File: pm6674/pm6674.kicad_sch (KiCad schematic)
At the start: 35 parts, among them IC101 ADR434BRZ, J101 Conn_01x10_Pin, U101 LM317_SOT-223, X101 CTS 970

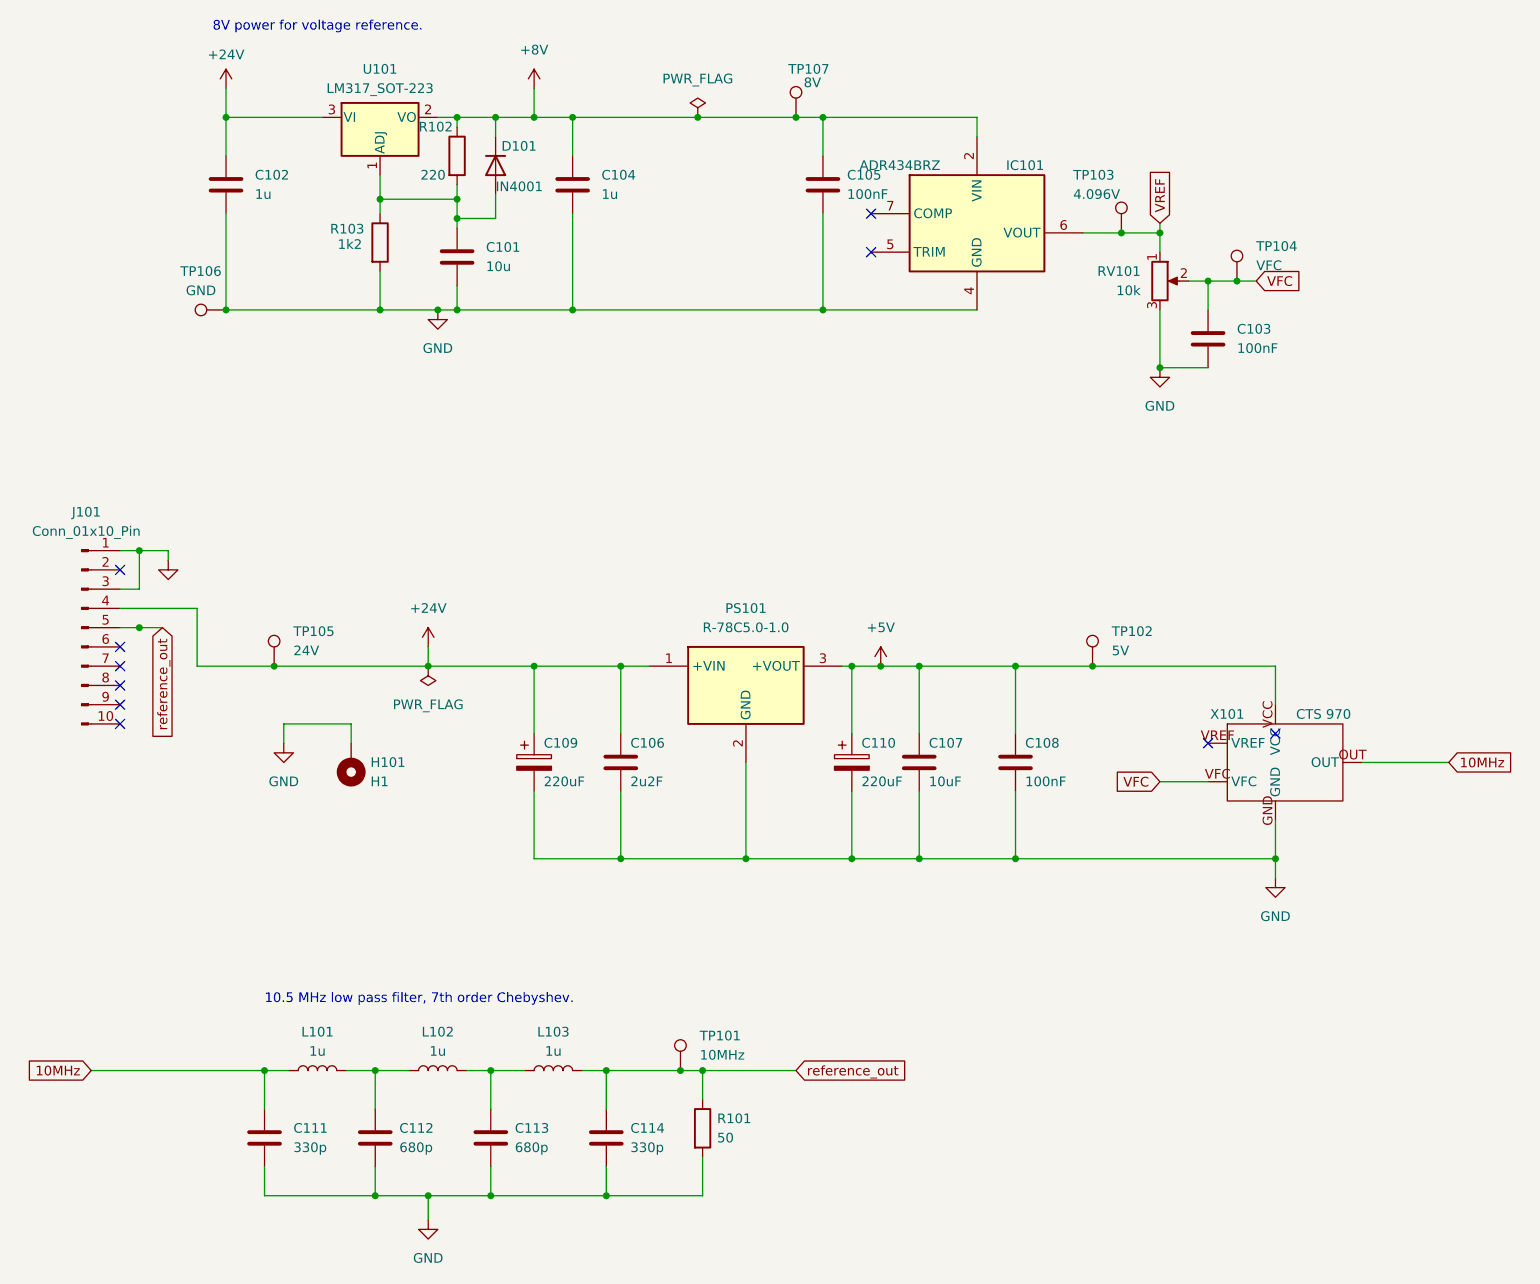
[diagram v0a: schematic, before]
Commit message: Final schematics of built-up and tested board.
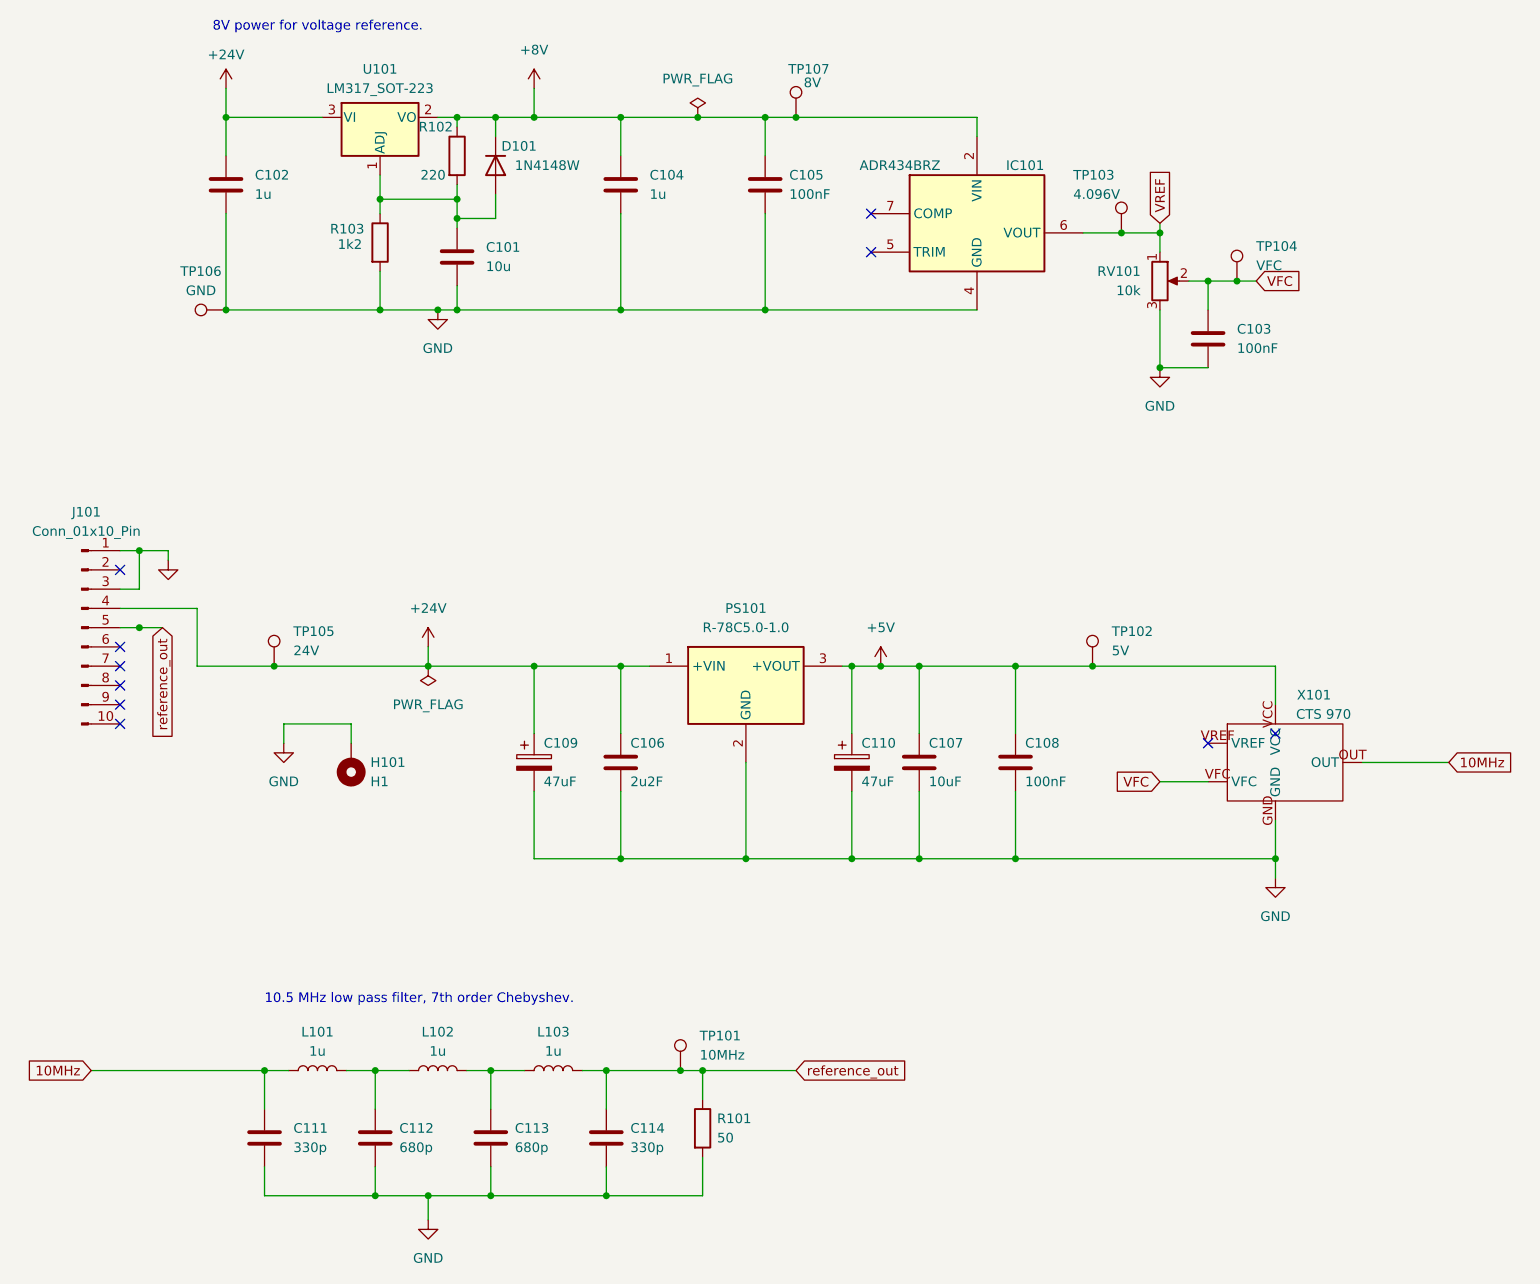
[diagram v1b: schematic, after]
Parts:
- C109, C110: value 220uF -> 47uF
- D101: value IN4001 -> 1N4148W
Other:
- company: Statsøkonomen -> Erik Ø. Sørensen, LB3TH
- moved on the sheet: C104, C105
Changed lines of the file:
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@@
   (title_block
     (title "10MHz reference board for Philips counter PM6674")
-    (company "Statsøkonomen")
+    (date "2023-12-20")
+    (company "Erik Ø. Sørensen, LB3TH")
+    (comment 1 "Inspiration (and physical measurements) from The Sync Channel Blog.")
+    (comment 2 "https://syncchannel.blogspot.com/2016/04/flukephilips-pm66xx-frequency-counter.html")
   )
   (junction (at 162.56 104.14) (diameter 0) (color 0 0 0 0)
@@
   (junction (at 78.105 157.48) (diameter 0) (color 0 0 0 0)
   )
+  (junction (at 129.54 31.75) (diameter 0) (color 0 0 0 0)
+  )
   (junction (at 187.96 53.34) (diameter 0) (color 0 0 0 0)
   )
-  (junction (at 104.14 31.75) (diameter 0) (color 0 0 0 0)
-  )
-  (junction (at 104.14 57.15) (diameter 0) (color 0 0 0 0)
-  )
   (junction (at 181.61 64.77) (diameter 0) (color 0 0 0 0)
   )
@@
   (junction (at 133.604 31.75) (diameter 0) (color 0 0 0 0)
   )
+  (junction (at 110.49 31.75) (diameter 0) (color 0 0 0 0)
+  )
   (junction (at 108.585 157.48) (diameter 0) (color 0 0 0 0)
   )
-  (junction (at 137.16 31.75) (diameter 0) (color 0 0 0 0)
-  )
   (junction (at 88.9 31.75) (diameter 0) (color 0 0 0 0)
   )
   (junction (at 144.78 104.14) (diameter 0) (color 0 0 0 0)
   )
+  (junction (at 110.49 57.15) (diameter 0) (color 0 0 0 0)
+  )
   (junction (at 88.9 42.545) (diameter 0) (color 0 0 0 0)
   )
@@
   (junction (at 108.585 173.99) (diameter 0) (color 0 0 0 0)
   )
+  (junction (at 129.54 57.15) (diameter 0) (color 0 0 0 0)
+  )
   (junction (at 176.53 46.99) (diameter 0) (color 0 0 0 0)
   )
@@
   )
   (junction (at 88.9 57.15) (diameter 0) (color 0 0 0 0)
-  )
-  (junction (at 137.16 57.15) (diameter 0) (color 0 0 0 0)
   )
   (junction (at 110.49 129.54) (diameter 0) (color 0 0 0 0)
@@
   (no_connect (at 187.96 114.3))
   (no_connect (at 44.45 101.6))
-  (wire (pts (xy 88.9 57.15) (xy 104.14 57.15))
+  (wire (pts (xy 88.9 57.15) (xy 110.49 57.15))
     (stroke (width 0) (type default))
   )
@@
     (stroke (width 0) (type default))
   )
-  (wire (pts (xy 133.604 31.75) (xy 137.16 31.75))
+  (wire (pts (xy 129.54 31.75) (xy 133.604 31.75))
+    (stroke (width 0) (type default))
+  )
+  (wire (pts (xy 110.49 57.15) (xy 129.54 57.15))
     (stroke (width 0) (type default))
   )
@@
     (stroke (width 0) (type default))
   )
-  (wire (pts (xy 99.06 31.75) (xy 104.14 31.75))
+  (wire (pts (xy 99.06 31.75) (xy 110.49 31.75))
     (stroke (width 0) (type default))
   )
@@
     (stroke (width 0) (type default))
   )
-  (wire (pts (xy 137.16 31.75) (xy 157.48 31.75))
-    (stroke (width 0) (type default))
-  )
   (wire (pts (xy 74.93 114.3) (xy 74.93 111.76))
     (stroke (width 0) (type default))
@@
     (stroke (width 0) (type default))
   )
-  (wire (pts (xy 137.16 44.45) (xy 137.16 57.15))
+  (wire (pts (xy 129.54 44.45) (xy 129.54 57.15))
     (stroke (width 0) (type default))
   )
@@
     (stroke (width 0) (type default))
   )
+  (wire (pts (xy 133.604 31.75) (xy 157.48 31.75))
+    (stroke (width 0) (type default))
+  )
   (wire (pts (xy 50.038 99.06) (xy 46.99 99.06))
     (stroke (width 0) (type default))
@@
     (stroke (width 0) (type default))
   )
-  (wire (pts (xy 137.16 36.83) (xy 137.16 31.75))
+  (wire (pts (xy 129.54 36.83) (xy 129.54 31.75))
     (stroke (width 0) (type default))
   )
@@
     (stroke (width 0) (type default))
   )
+  (wire (pts (xy 110.49 31.75) (xy 120.65 31.75))
+    (stroke (width 0) (type default))
+  )
   (wire (pts (xy 110.49 104.14) (xy 110.49 113.03))
     (stroke (width 0) (type default))
@@
     (stroke (width 0) (type default))
   )
-  (wire (pts (xy 120.65 31.75) (xy 133.604 31.75))
+  (wire (pts (xy 120.65 31.75) (xy 129.54 31.75))
     (stroke (width 0) (type default))
   )
@@
     (stroke (width 0) (type default))
   )
-  (wire (pts (xy 104.14 57.15) (xy 137.16 57.15))
-    (stroke (width 0) (type default))
-  )
   (wire (pts (xy 108.585 157.48) (xy 108.585 162.56))
     (stroke (width 0) (type default))
@@
     (stroke (width 0) (type default))
   )
-  (wire (pts (xy 104.14 44.45) (xy 104.14 57.15))
+  (wire (pts (xy 110.49 44.45) (xy 110.49 57.15))
     (stroke (width 0) (type default))
   )
@@
     (stroke (width 0) (type default))
   )
-  (wire (pts (xy 104.14 31.75) (xy 104.14 36.83))
+  (wire (pts (xy 129.54 57.15) (xy 157.48 57.15))
+    (stroke (width 0) (type default))
+  )
+  (wire (pts (xy 110.49 31.75) (xy 110.49 36.83))
     (stroke (width 0) (type default))
   )
@@
     (stroke (width 0) (type default))
   )
-  (wire (pts (xy 104.14 31.75) (xy 120.65 31.75))
-    (stroke (width 0) (type default))
-  )
   (wire (pts (xy 78.74 57.15) (xy 86.36 57.15))
-    (stroke (width 0) (type default))
-  )
-  (wire (pts (xy 137.16 57.15) (xy 157.48 57.15))
     (stroke (width 0) (type default))
   )
@@
     )
   )
-  (symbol (lib_id "Device:C") (at 104.14 40.64 0) (unit 1)
-    (in_bom yes) (on_board yes) (dnp no) (fields_autoplaced)
-    (property "Reference" "C104" (at 107.95 39.37 0)
-      (effects (font (size 1.27 1.27)) (justify left))
-    )
-    (property "Value" "1u" (at 107.95 41.91 0)
-      (effects (font (size 1.27 1.27)) (justify left))
-    )
-    (property "Footprint" "Capacitor_SMD:C_0805_2012Metric" (at 105.1052 44.45 0)
-      (effects (font (size 1.27 1.27)) hide)
-    )
-    (property "Datasheet" "~" (at 104.14 40.64 0)
+  (symbol (lib_id "Device:C") (at 110.49 40.64 0) (unit 1)
+    (in_bom yes) (on_board yes) (dnp no) (fields_autoplaced)
+    (property "Reference" "C104" (at 114.3 39.37 0)
+      (effects (font (size 1.27 1.27)) (justify left))
+    )
+    (property "Value" "1u" (at 114.3 41.91 0)
+      (effects (font (size 1.27 1.27)) (justify left))
+    )
+    (property "Footprint" "Capacitor_SMD:C_0805_2012Metric" (at 111.4552 44.45 0)
+      (effects (font (size 1.27 1.27)) hide)
+    )
+    (property "Datasheet" "~" (at 110.49 40.64 0)
       (effects (font (size 1.27 1.27)) hide)
     )
@@
       (effects (font (size 1.27 1.27)) (justify left))
     )
-    (property "Value" "IN4001" (at 93.98 40.894 90)
+    (property "Value" "1N4148W" (at 96.52 38.1 90)
       (effects (font (size 1.27 1.27)) (justify left))
     )
@@
   (symbol (lib_id "lb3th:CTS1950017") (at 196.85 114.3 0) (unit 1)
     (in_bom yes) (on_board yes) (dnp no)
-    (property "Reference" "X101" (at 190.5 110.49 0)
+    (property "Reference" "X101" (at 201.93 107.95 0)
       (effects (font (size 1.27 1.27)))
     )
@@
     )
   )
-  (symbol (lib_id "Device:C") (at 137.16 40.64 0) (unit 1)
-    (in_bom yes) (on_board yes) (dnp no) (fields_autoplaced)
-    (property "Reference" "C105" (at 140.335 39.37 0)
-      (effects (font (size 1.27 1.27)) (justify left))
-    )
-    (property "Value" "100nF" (at 140.335 41.91 0)
-      (effects (font (size 1.27 1.27)) (justify left))
-    )
-    (property "Footprint" "Capacitor_SMD:C_0805_2012Metric" (at 138.1252 44.45 0)
-      (effects (font (size 1.27 1.27)) hide)
-    )
-    (property "Datasheet" "~" (at 137.16 40.64 0)
+  (symbol (lib_id "Device:C") (at 129.54 40.64 0) (unit 1)
+    (in_bom yes) (on_board yes) (dnp no) (fields_autoplaced)
+    (property "Reference" "C105" (at 132.715 39.37 0)
+      (effects (font (size 1.27 1.27)) (justify left))
+    )
+    (property "Value" "100nF" (at 132.715 41.91 0)
+      (effects (font (size 1.27 1.27)) (justify left))
+    )
+    (property "Footprint" "Capacitor_SMD:C_0805_2012Metric" (at 130.5052 44.45 0)
+      (effects (font (size 1.27 1.27)) hide)
+    )
+    (property "Datasheet" "~" (at 129.54 40.64 0)
       (effects (font (size 1.27 1.27)) hide)
     )
@@
       (effects (font (size 1.27 1.27)) (justify left))
     )
-    (property "Value" "220uF" (at 100.33 119.38 0)
+    (property "Value" "47uF" (at 100.33 119.38 0)
       (effects (font (size 1.27 1.27)) (justify left))
     )
@@
       (effects (font (size 1.27 1.27)) (justify left))
     )
-    (property "Value" "220uF" (at 142.24 119.38 0)
-      (effects (font (size 1.27 1.27)) (justify left))
-    )
+    (property "Value" "47uF" (at 142.24 119.38 0)
+      (effects (font (size 1.27 1.27)) (justify left))
+    )
